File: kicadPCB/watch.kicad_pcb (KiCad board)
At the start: 2 copper layers, 81 x 53 mm, 64 parts, among them IC1 ISL1209, J2 USB-MICROB, M1 BOS_LIBS_SWD_BREAKOUTS, T1 BC850, U2 MKL27Z256VLH4, Y1 Crystal

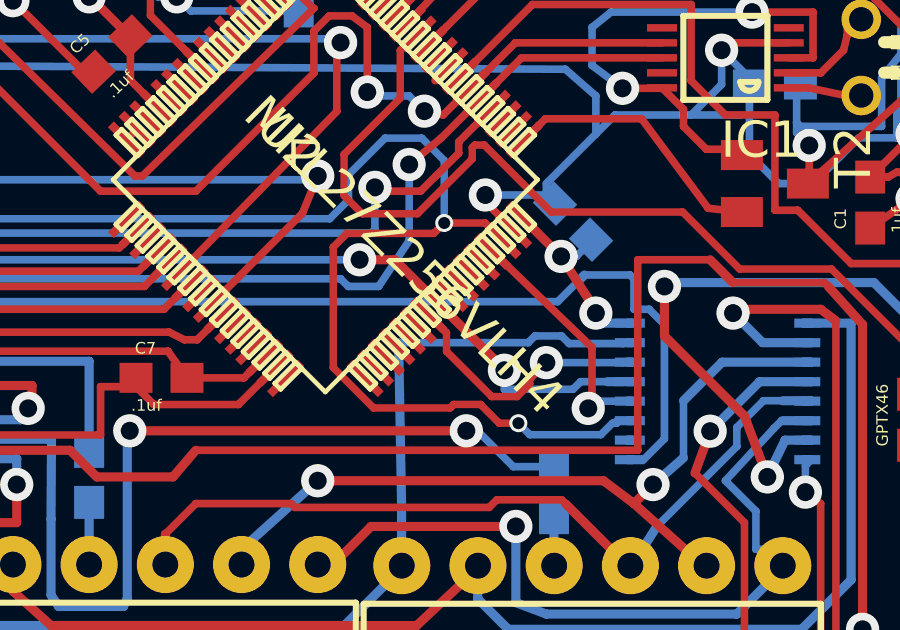
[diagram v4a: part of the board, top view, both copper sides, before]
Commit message: moved OE to a timer pin to control display brightness
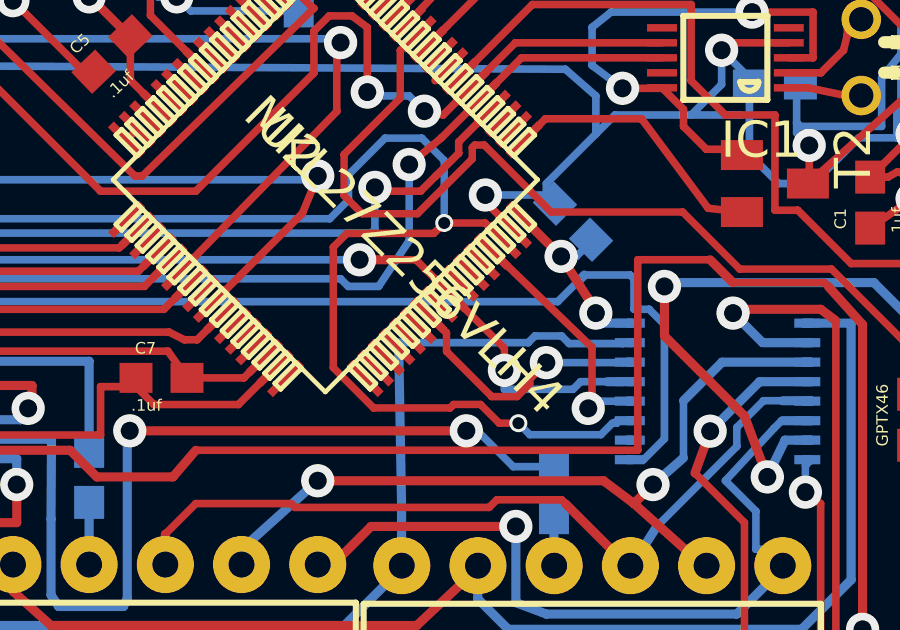
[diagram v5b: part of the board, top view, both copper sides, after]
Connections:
- U$4 pad OE: /PTB17 -> /PTB18
- U$5 pad OE: /PTB17 -> /PTB18
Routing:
- net /PTB18: track 0.00 -> 44.1 mm, vias 0 -> 2
- net /PTB17: track 43.7 -> 0.00 mm, vias 2 -> 0
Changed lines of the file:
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@@
     (thickness 1.6)
     (drawings 87)
-    (tracks 820)
+    (tracks 822)
     (zones 0)
     (modules 64)
@@
       (net 111 /PTB16))
     (pad OE smd rect (at 3.38 0 180) (size 0.6096 0.3048) (layers Bottom B.Paste B.Mask)
-      (net 64 /PTB17))
+      (net 112 /PTB18))
     (pad STCP smd rect (at 3.38 -0.65 180) (size 0.6096 0.3048) (layers Bottom B.Paste B.Mask)
       (net 65 /PTC2))
@@
       (net 68 /N$28))
     (pad OE smd rect (at 3.38 0 180) (size 0.6096 0.3048) (layers Bottom B.Paste B.Mask)
-      (net 64 /PTB17))
+      (net 112 /PTB18))
     (pad STCP smd rect (at 3.38 -0.65 180) (size 0.6096 0.3048) (layers Bottom B.Paste B.Mask)
       (net 69 /PTC7))
@@
   (segment (start 119.423244 98.847558) (end 119.423244 102.356211) (width 0.254) (layer Top) (net 62))
   (segment (start 119.423244 102.356211) (end 121.897769 104.957736) (width 0.254) (layer Top) (net 62))
-  (segment (start 128.997244 104.534589) (end 125.519244 104.534589) (width 0.3048) (layer Bottom) (net 64))
-  (segment (start 125.519244 104.534589) (end 125.519244 99.073589) (width 0.3048) (layer Bottom) (net 64))
-  (segment (start 148.887244 99.073589) (end 148.887244 99.200589) (width 0.3048) (layer Bottom) (net 64))
-  (via (at 148.887244 99.200589) (size 1.108) (drill 0.6) (layers Top Bottom) (net 64))
-  (segment (start 148.887244 99.200589) (end 150.057703 99.200589) (width 0.3048) (layer Top) (net 64))
-  (segment (start 150.057703 99.200589) (end 151.544953 100.687839) (width 0.3048) (layer Top) (net 64))
-  (via (at 153.713244 102.883589) (size 1.108) (drill 0.6) (layers Top Bottom) (net 64))
-  (segment (start 153.713244 102.883589) (end 153.740703 102.883589) (width 0.3048) (layer Top) (net 64))
-  (segment (start 153.740703 102.883589) (end 151.544953 100.687839) (width 0.3048) (layer Top) (net 64))
-  (segment (start 157.142244 103.264589) (end 157.699244 103.264589) (width 0.3048) (layer Bottom) (net 64))
-  (segment (start 153.713244 102.883589) (end 153.713244 103.518589) (width 0.254) (layer Bottom) (net 64))
-  (segment (start 153.713244 103.518589) (end 155.999244 103.518589) (width 0.254) (layer Bottom) (net 64))
-  (segment (start 155.999244 103.518589) (end 156.253244 103.264589) (width 0.254) (layer Bottom) (net 64))
-  (segment (start 156.253244 103.264589) (end 157.142244 103.264589) (width 0.254) (layer Bottom) (net 64))
-  (segment (start 127.805244 99.200589) (end 148.887244 99.200589) (width 0.254) (layer Bottom) (net 64))
-  (segment (start 125.519244 99.073589) (end 126.281244 99.073589) (width 0.254) (layer Bottom) (net 64))
-  (segment (start 126.281244 99.073589) (end 126.408244 98.946589) (width 0.254) (layer Bottom) (net 64))
-  (segment (start 126.408244 98.946589) (end 127.551244 98.946589) (width 0.254) (layer Bottom) (net 64))
-  (segment (start 127.551244 98.946589) (end 127.805244 99.200589) (width 0.254) (layer Bottom) (net 64))
   (segment (start 157.699244 103.914589) (end 156.873244 103.914589) (width 0.254) (layer Bottom) (net 65))
   (segment (start 156.873244 103.914589) (end 156.507244 104.153589) (width 0.254) (layer Bottom) (net 65))
@@
   (via (at 155.110244 102.629589) (size 1.108) (drill 0.6) (layers Top Bottom) (net 111))
   (segment (start 155.110244 102.629589) (end 154.773919 102.629589) (width 0.254) (layer Top) (net 111))
+  (segment (start 151.898492 100.334301) (end 153.713244 102.149053) (width 0.25) (layer Top) (net 112))
+  (segment (start 153.713244 102.149053) (end 153.713244 102.883589) (width 0.25) (layer Top) (net 112))
+  (segment (start 151.898492 100.334301) (end 150.76478 99.200589) (width 0.25) (layer Top) (net 112))
+  (segment (start 150.76478 99.200589) (end 150.057703 99.200589) (width 0.25) (layer Top) (net 112))
+  (segment (start 128.997244 104.534589) (end 125.519244 104.534589) (width 0.3048) (layer Bottom) (net 112))
+  (segment (start 125.519244 104.534589) (end 125.519244 99.073589) (width 0.3048) (layer Bottom) (net 112))
+  (segment (start 148.887244 99.073589) (end 148.887244 99.200589) (width 0.3048) (layer Bottom) (net 112))
+  (via (at 148.887244 99.200589) (size 1.108) (drill 0.6) (layers Top Bottom) (net 112))
+  (segment (start 148.887244 99.200589) (end 150.057703 99.200589) (width 0.3048) (layer Top) (net 112))
+  (via (at 153.713244 102.883589) (size 1.108) (drill 0.6) (layers Top Bottom) (net 112))
+  (segment (start 153.713244 102.883589) (end 153.740703 102.883589) (width 0.3048) (layer Top) (net 112))
+  (segment (start 157.142244 103.264589) (end 157.699244 103.264589) (width 0.3048) (layer Bottom) (net 112))
+  (segment (start 153.713244 102.883589) (end 153.713244 103.518589) (width 0.254) (layer Bottom) (net 112))
+  (segment (start 153.713244 103.518589) (end 155.999244 103.518589) (width 0.254) (layer Bottom) (net 112))
+  (segment (start 155.999244 103.518589) (end 156.253244 103.264589) (width 0.254) (layer Bottom) (net 112))
+  (segment (start 156.253244 103.264589) (end 157.142244 103.264589) (width 0.254) (layer Bottom) (net 112))
+  (segment (start 127.805244 99.200589) (end 148.887244 99.200589) (width 0.254) (layer Bottom) (net 112))
+  (segment (start 125.519244 99.073589) (end 126.281244 99.073589) (width 0.254) (layer Bottom) (net 112))
+  (segment (start 126.281244 99.073589) (end 126.408244 98.946589) (width 0.254) (layer Bottom) (net 112))
+  (segment (start 126.408244 98.946589) (end 127.551244 98.946589) (width 0.254) (layer Bottom) (net 112))
+  (segment (start 127.551244 98.946589) (end 127.805244 99.200589) (width 0.254) (layer Bottom) (net 112))
   (segment (start 172.72 120.396) (end 172.72 94.647343) (width 0.25) (layer Top) (net 117))
   (segment (start 172.72 94.647343) (end 170.841245 92.768588) (width 0.25) (layer Top) (net 117))
